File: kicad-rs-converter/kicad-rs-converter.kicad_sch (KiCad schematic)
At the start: 29 parts

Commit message: Scheme annotation
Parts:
- gave numbers to parts that had none: 29
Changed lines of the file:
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@@
 		(on_board yes)
 		(dnp no)
-		(property "Reference" "C?"
+		(property "Reference" "C2"
 			(at 77.724 92.202 90)
 			(effects
@@
 			(project ""
 				(path "/bc93e02f-9da6-4af9-a56b-db2eb76f1927"
-					(reference "C?")
+					(reference "C2")
 					(unit 1)
 				)
@@
 		(dnp no)
 		(fields_autoplaced yes)
-		(property "Reference" "HL?"
+		(property "Reference" "HL2"
 			(at 215.9 122.8725 0)
 			(effects
@@
 			(project ""
 				(path "/bc93e02f-9da6-4af9-a56b-db2eb76f1927"
-					(reference "HL?")
+					(reference "HL2")
 					(unit 1)
 				)
@@
 		(on_board yes)
 		(dnp no)
-		(property "Reference" "R?"
+		(property "Reference" "R4"
 			(at 137.16 32.385 90)
 			(effects
@@
 			(project ""
 				(path "/bc93e02f-9da6-4af9-a56b-db2eb76f1927"
-					(reference "R?")
+					(reference "R4")
 					(unit 1)
 				)
@@
 		(dnp no)
 		(fields_autoplaced yes)
-		(property "Reference" "R?"
+		(property "Reference" "R8"
 			(at 241.3 83.185 90)
 			(effects
@@
 			(project ""
 				(path "/bc93e02f-9da6-4af9-a56b-db2eb76f1927"
-					(reference "R?")
+					(reference "R8")
 					(unit 1)
 				)
@@
 		(on_board yes)
 		(dnp no)
-		(property "Reference" "C?"
+		(property "Reference" "C3"
 			(at 136.652 74.422 90)
 			(effects
@@
 			(project ""
 				(path "/bc93e02f-9da6-4af9-a56b-db2eb76f1927"
-					(reference "C?")
+					(reference "C3")
 					(unit 1)
 				)
@@
 		(dnp no)
 		(fields_autoplaced yes)
-		(property "Reference" "DD?"
+		(property "Reference" "DD2"
 			(at 199.39 58.42 0)
 			(effects
@@
 			(project ""
 				(path "/bc93e02f-9da6-4af9-a56b-db2eb76f1927"
-					(reference "DD?")
+					(reference "DD2")
 					(unit 1)
 				)
@@
 		(on_board yes)
 		(dnp no)
-		(property "Reference" "R?"
+		(property "Reference" "R7"
 			(at 234.95 59.69 0)
 			(effects
@@
 			(project ""
 				(path "/bc93e02f-9da6-4af9-a56b-db2eb76f1927"
-					(reference "R?")
+					(reference "R7")
 					(unit 1)
 				)
@@
 		(dnp no)
 		(fields_autoplaced yes)
-		(property "Reference" "DD?"
+		(property "Reference" "DD1"
 			(at 109.22 68.58 0)
 			(effects
@@
 			(project ""
 				(path "/bc93e02f-9da6-4af9-a56b-db2eb76f1927"
-					(reference "DD?")
+					(reference "DD1")
 					(unit 1)
 				)
@@
 		(on_board yes)
 		(dnp no)
-		(property "Reference" "C?"
+		(property "Reference" "C1"
 			(at 61.722 82.296 90)
 			(effects
@@
 			(project ""
 				(path "/bc93e02f-9da6-4af9-a56b-db2eb76f1927"
-					(reference "C?")
+					(reference "C1")
 					(unit 1)
 				)
@@
 		(on_board yes)
 		(dnp no)
-		(property "Reference" "C?"
+		(property "Reference" "C5"
 			(at 193.802 21.59 0)
 			(effects
@@
 			(project ""
 				(path "/bc93e02f-9da6-4af9-a56b-db2eb76f1927"
-					(reference "C?")
+					(reference "C5")
 					(unit 1)
 				)
@@
 		(on_board yes)
 		(dnp no)
-		(property "Reference" "C?"
+		(property "Reference" "C4"
 			(at 149.352 84.328 90)
 			(effects
@@
 			(project ""
 				(path "/bc93e02f-9da6-4af9-a56b-db2eb76f1927"
-					(reference "C?")
+					(reference "C4")
 					(unit 1)
 				)
@@
 		(dnp no)
 		(fields_autoplaced yes)
-		(property "Reference" "DA?"
+		(property "Reference" "DA1"
 			(at 223.52 11.43 0)
 			(effects
@@
 			(project ""
 				(path "/bc93e02f-9da6-4af9-a56b-db2eb76f1927"
-					(reference "DA?")
+					(reference "DA1")
 					(unit 1)
 				)
@@
 		(on_board yes)
 		(dnp no)
-		(property "Reference" "XS?"
+		(property "Reference" "XS3"
 			(at 266.7 88.138 0)
 			(effects
@@
 			(project ""
 				(path "/bc93e02f-9da6-4af9-a56b-db2eb76f1927"
-					(reference "XS?")
+					(reference "XS3")
 					(unit 1)
 				)
@@
 		(dnp no)
 		(fields_autoplaced yes)
-		(property "Reference" "R?"
+		(property "Reference" "R1"
 			(at 80.01 146.685 90)
 			(effects
@@
 			(project ""
 				(path "/bc93e02f-9da6-4af9-a56b-db2eb76f1927"
-					(reference "R?")
+					(reference "R1")
 					(unit 1)
 				)
@@
 		(dnp no)
 		(fields_autoplaced yes)
-		(property "Reference" "R?"
+		(property "Reference" "R6"
 			(at 207.01 102.235 90)
 			(effects
@@
 			(project ""
 				(path "/bc93e02f-9da6-4af9-a56b-db2eb76f1927"
-					(reference "R?")
+					(reference "R6")
 					(unit 1)
 				)
@@
 		(dnp no)
 		(fields_autoplaced yes)
-		(property "Reference" "R?"
+		(property "Reference" "R11"
 			(at 275.59 65.405 90)
 			(effects
@@
 			(project ""
 				(path "/bc93e02f-9da6-4af9-a56b-db2eb76f1927"
-					(reference "R?")
+					(reference "R11")
 					(unit 1)
 				)
@@
 		(dnp no)
 		(fields_autoplaced yes)
-		(property "Reference" "VT?"
+		(property "Reference" "VT1"
 			(at 118.11 19.05 90)
 			(effects
@@
 			(project ""
 				(path "/bc93e02f-9da6-4af9-a56b-db2eb76f1927"
-					(reference "VT?")
+					(reference "VT1")
 					(unit 1)
 				)
@@
 		(dnp no)
 		(fields_autoplaced yes)
-		(property "Reference" "R?"
+		(property "Reference" "R10"
 			(at 259.08 45.72 0)
 			(effects
@@
 			(project ""
 				(path "/bc93e02f-9da6-4af9-a56b-db2eb76f1927"
-					(reference "R?")
+					(reference "R10")
 					(unit 1)
 				)
@@
 		(on_board yes)
 		(dnp no)
-		(property "Reference" "C?"
+		(property "Reference" "C8"
 			(at 255.016 21.59 0)
 			(effects
@@
 			(project ""
 				(path "/bc93e02f-9da6-4af9-a56b-db2eb76f1927"
-					(reference "C?")
+					(reference "C8")
 					(unit 1)
 				)
@@
 		(dnp no)
 		(fields_autoplaced yes)
-		(property "Reference" "VD?"
+		(property "Reference" "VD1"
 			(at 180.34 12.7 0)
 			(effects
@@
 			(project ""
 				(path "/bc93e02f-9da6-4af9-a56b-db2eb76f1927"
-					(reference "VD?")
+					(reference "VD1")
 					(unit 1)
 				)
@@
 		(on_board yes)
 		(dnp no)
-		(property "Reference" "XS?"
+		(property "Reference" "XS1"
 			(at 35.052 98.044 0)
 			(effects
@@
 			(project ""
 				(path "/bc93e02f-9da6-4af9-a56b-db2eb76f1927"
-					(reference "XS?")
+					(reference "XS1")
 					(unit 1)
 				)
@@
 		(on_board yes)
 		(dnp no)
-		(property "Reference" "R?"
+		(property "Reference" "R2"
 			(at 105.41 32.385 90)
 			(effects
@@
 			(project ""
 				(path "/bc93e02f-9da6-4af9-a56b-db2eb76f1927"
-					(reference "R?")
+					(reference "R2")
 					(unit 1)
 				)
@@
 		(on_board yes)
 		(dnp no)
-		(property "Reference" "C?"
+		(property "Reference" "C7"
 			(at 238.506 21.082 0)
 			(effects
@@
 			(project ""
 				(path "/bc93e02f-9da6-4af9-a56b-db2eb76f1927"
-					(reference "C?")
+					(reference "C7")
 					(unit 1)
 				)
@@
 		(on_board yes)
 		(dnp no)
-		(property "Reference" "R?"
+		(property "Reference" "R3"
 			(at 120.142 40.64 90)
 			(effects
@@
 			(project ""
 				(path "/bc93e02f-9da6-4af9-a56b-db2eb76f1927"
-					(reference "R?")
+					(reference "R3")
 					(unit 1)
 				)
@@
 		(on_board yes)
 		(dnp no)
-		(property "Reference" "R?"
+		(property "Reference" "R5"
 			(at 147.574 38.608 0)
 			(effects
@@
 			(project ""
 				(path "/bc93e02f-9da6-4af9-a56b-db2eb76f1927"
-					(reference "R?")
+					(reference "R5")
 					(unit 1)
 				)
@@
 		(dnp no)
 		(fields_autoplaced yes)
-		(property "Reference" "R?"
+		(property "Reference" "R9"
 			(at 252.73 68.58 0)
 			(effects
@@
 			(project ""
 				(path "/bc93e02f-9da6-4af9-a56b-db2eb76f1927"
-					(reference "R?")
+					(reference "R9")
 					(unit 1)
 				)
@@
 		(on_board yes)
 		(dnp no)
-		(property "Reference" "C?"
+		(property "Reference" "C6"
 			(at 209.804 21.844 0)
 			(effects
@@
 			(project ""
 				(path "/bc93e02f-9da6-4af9-a56b-db2eb76f1927"
-					(reference "C?")
+					(reference "C6")
 					(unit 1)
 				)
@@
 		(dnp no)
 		(fields_autoplaced yes)
-		(property "Reference" "HL?"
+		(property "Reference" "HL1"
 			(at 88.9 167.3225 0)
 			(effects
@@
 			(project ""
 				(path "/bc93e02f-9da6-4af9-a56b-db2eb76f1927"
-					(reference "HL?")
+					(reference "HL1")
 					(unit 1)
 				)
@@
 		(on_board yes)
 		(dnp no)
-		(property "Reference" "XS?"
+		(property "Reference" "XS2"
 			(at 219.964 52.578 0)
 			(effects
@@
 			(project ""
 				(path "/bc93e02f-9da6-4af9-a56b-db2eb76f1927"
-					(reference "XS?")
-					(unit 1)
-				)
+					(reference "XS2")
+					(unit 1)
+				)

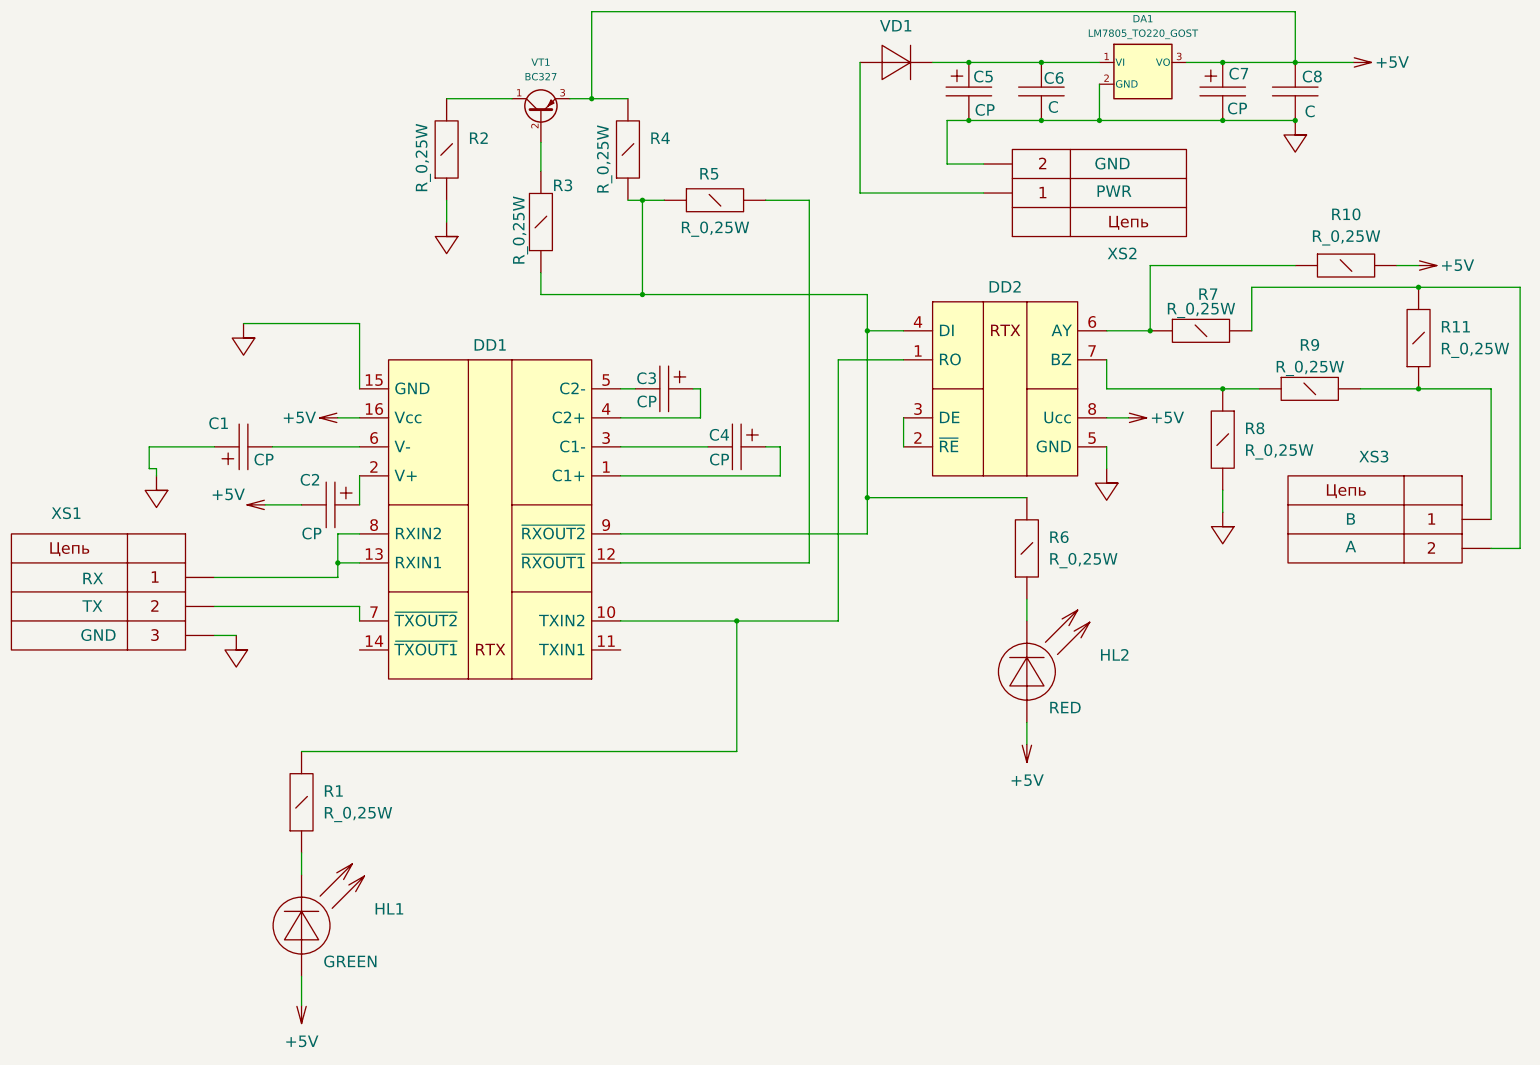
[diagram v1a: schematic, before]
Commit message: Placed values on every element
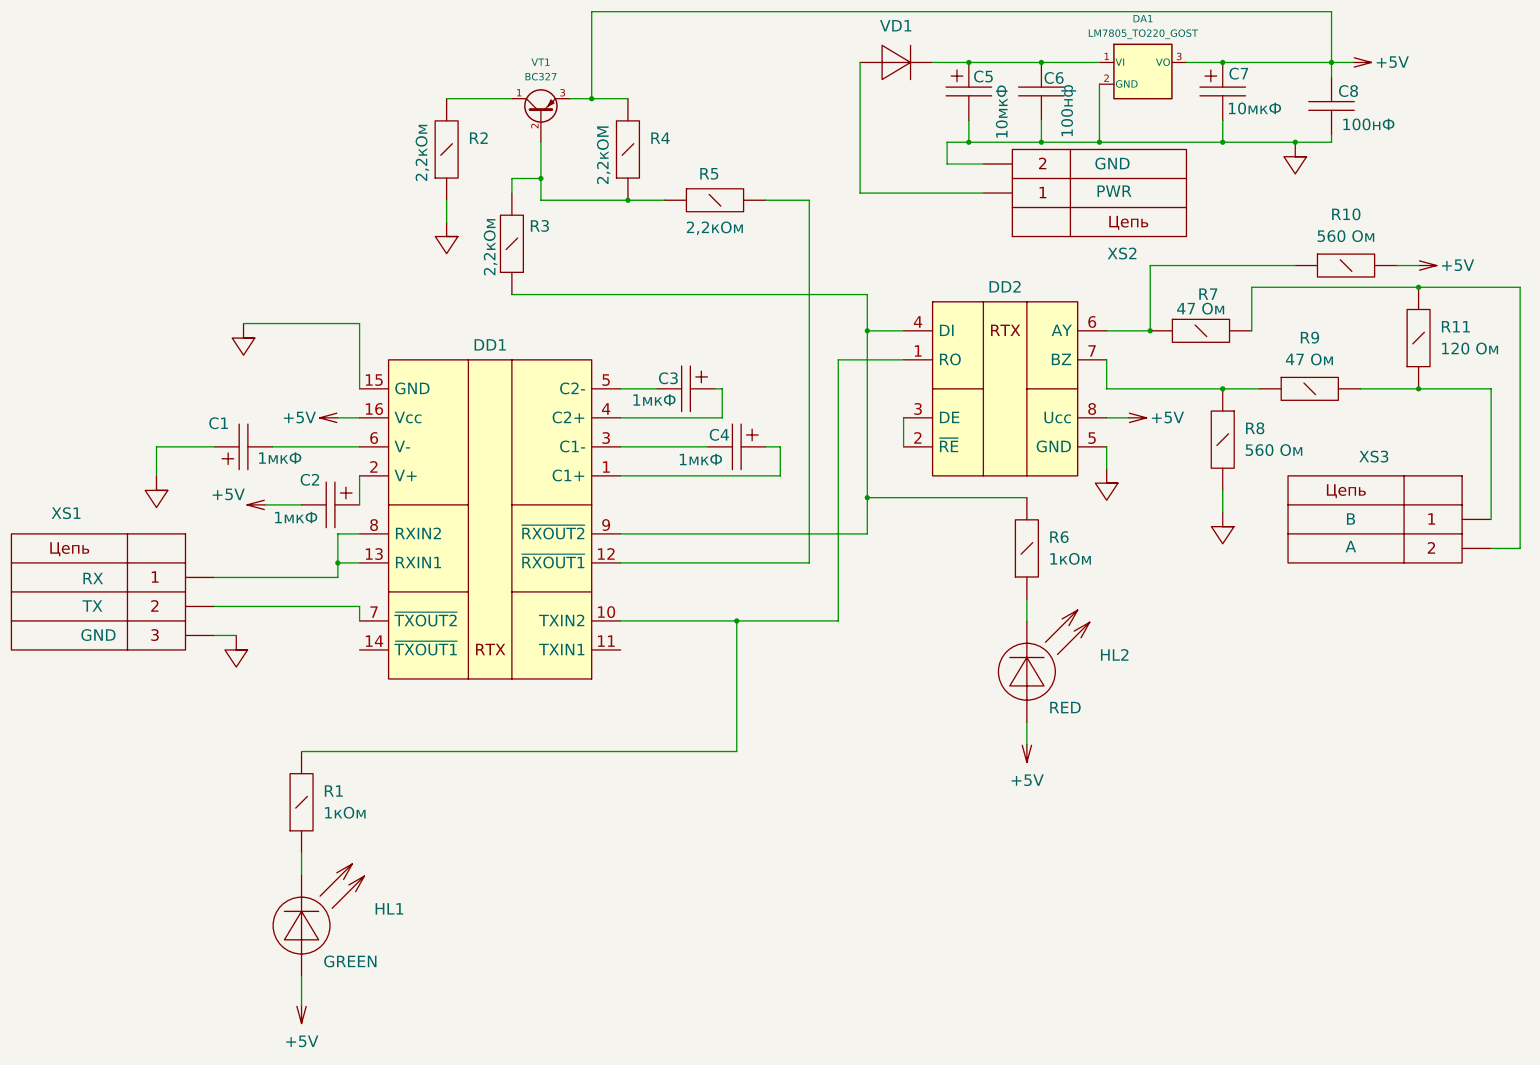
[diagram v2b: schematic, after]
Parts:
- C1, C2, C3, C4: value CP -> 1мкФ
- C5, C7: value CP -> 10мкФ
- C6: value C -> 100нф
- C8: value C -> 100нФ
- R1, R6: value R_0,25W -> 1кОм
- R10, R8: value R_0,25W -> 560 Ом
- R11: value R_0,25W -> 120 Ом
- R2, R3, R5: value R_0,25W -> 2,2кОм
- R4: value R_0,25W -> 2,2кОМ
- R7, R9: value R_0,25W -> 47 Ом
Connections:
- net at DD1.9 (~{RXOUT2}), DD2.4 (DI), R3.1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: no longer R4.1, R5.1
- net at R3.2, VT1.2 (B): now also R4.1, R5.1
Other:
- moved on the sheet: C3, C8, R3

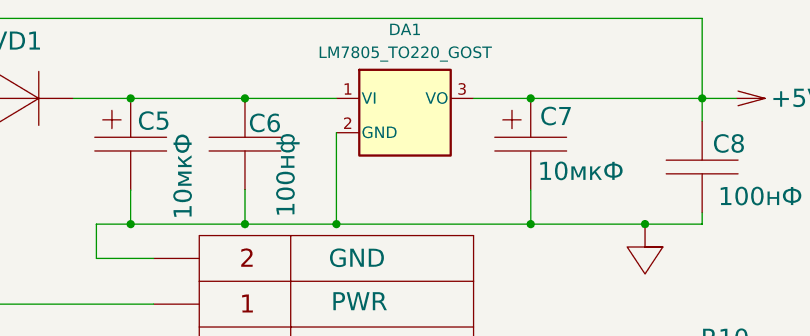
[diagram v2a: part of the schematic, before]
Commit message: s/LM7805_TO220_GOST/LM7805/
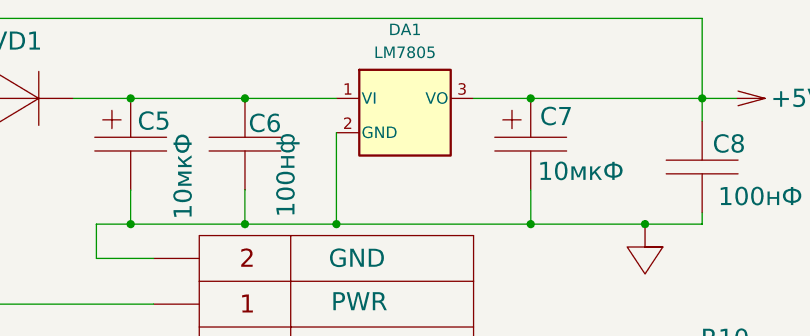
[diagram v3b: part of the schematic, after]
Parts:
- DA1: value LM7805_TO220_GOST -> LM7805
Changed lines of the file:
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@@
 			)
 		)
-		(property "Value" "LM7805_TO220_GOST"
+		(property "Value" "LM7805"
 			(at 223.52 13.97 0)
 			(effects

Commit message: MAX232 and MAX485 in my own library
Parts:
- DA1: value LM7805 -> LM7805_TO220_GOST
- DD1: symbol Interface_UART_GOST:5559ИН1Т -> kicad-rs-converter:MAX232_GOST
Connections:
- net at DD2.2 (~{RE}), DD2.3 (DE): now also R2.2, VT1.1 (C)
